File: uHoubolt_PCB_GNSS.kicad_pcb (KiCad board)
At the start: 4 copper layers, 85 x 80 mm, 89 parts, among them J1 Power In, J12 MMCX-J-P-H-RA-SM1, J2 Debug, J3 Debug, J4 CAN1, J5 CAN2, J6 CAN1, J7 CAN2, Q1 SISA88DN or similar, U1 SAM-M8Q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

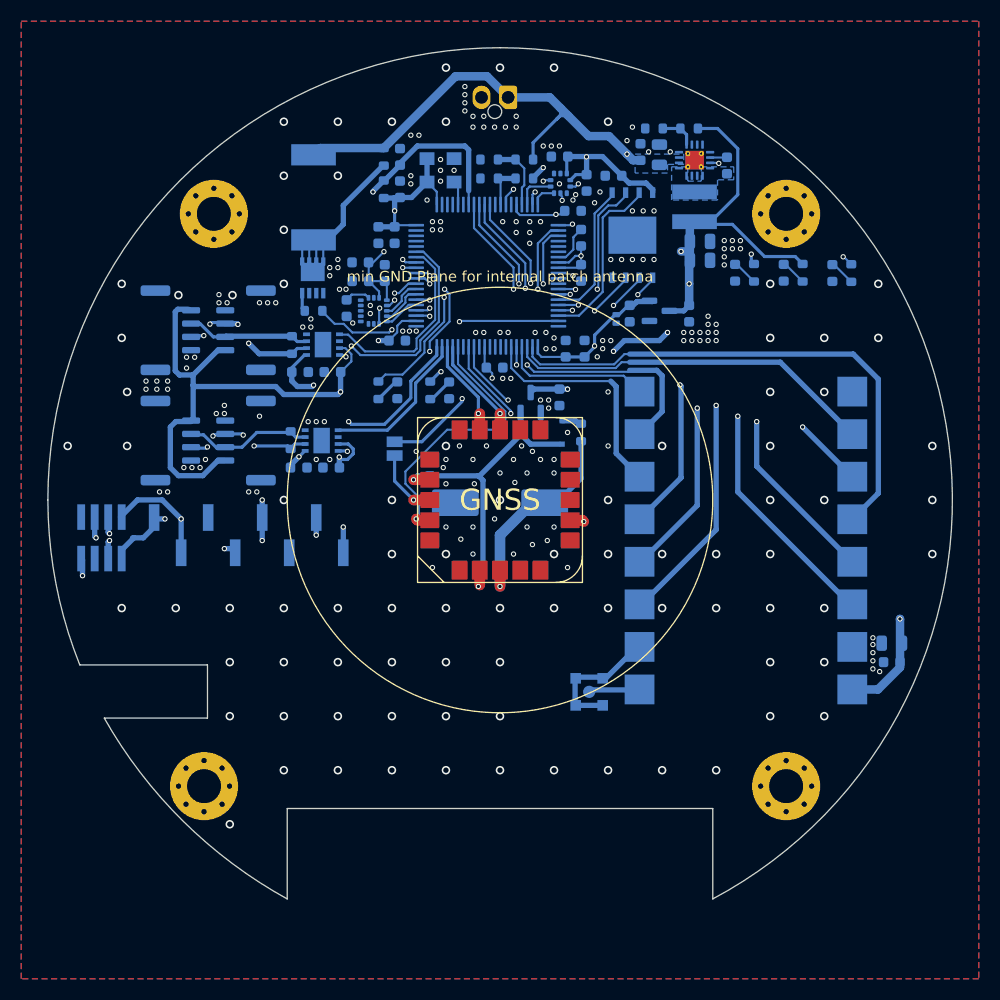
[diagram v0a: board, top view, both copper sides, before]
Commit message: Rounded board; updated LoRa module; Small bugfixes and rewiring
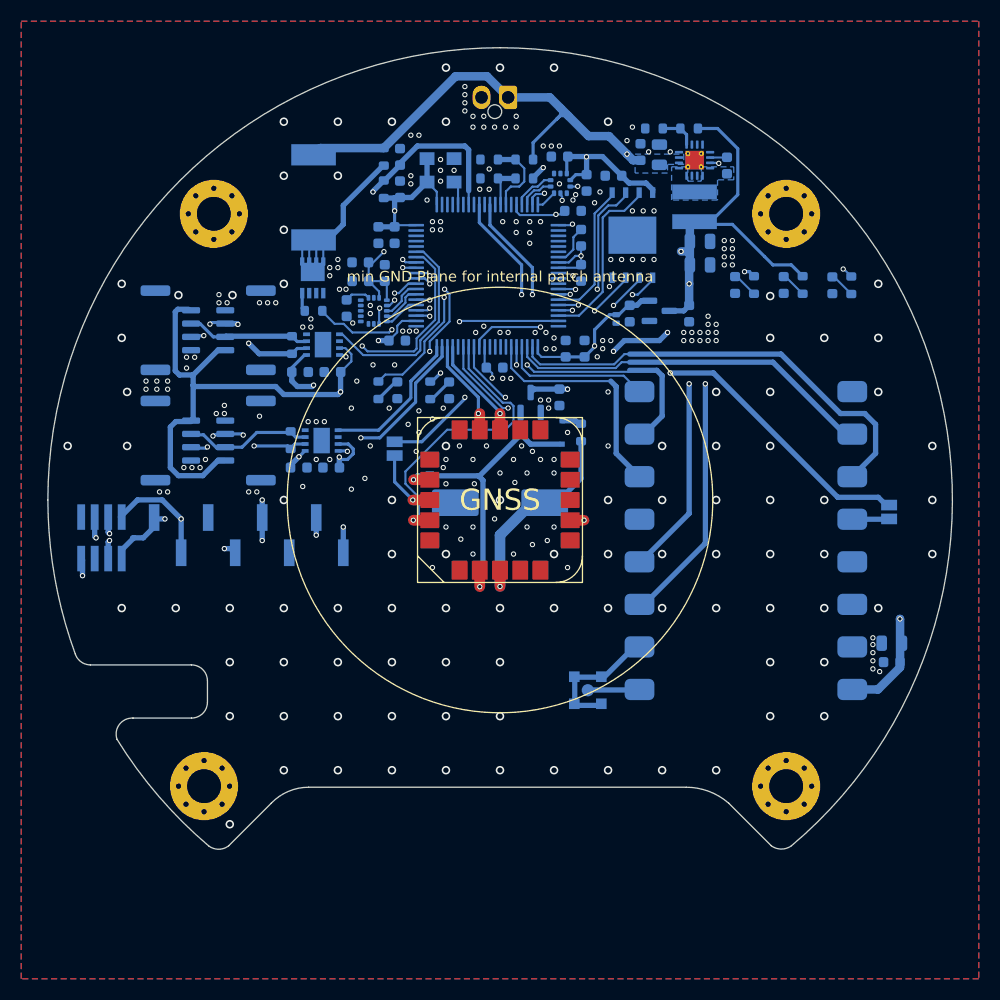
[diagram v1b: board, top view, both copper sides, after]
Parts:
- added JP2: SolderJumper_, Jumper:SolderJumper-2_P1.3mm_Open_Pad1.0x1.5mm, B.Cu at (186.6, 101.1)
- U10: value LoRa1278F30 -> LoRa1276F30; footprint TXV_Library_Footprints:G-NiceRF-LoRa1278F30 -> TXV_Library_Footprints:G-NiceRF-LoRa1268F30
- moved D3 1.15 mm to (176.7, 79.8)
- moved D5 1.15 mm to (172.1, 79.8)
- moved R14 1.15 mm to (178.4, 79.8)
- moved R17 1.15 mm to (173.9, 79.8)
- moved D1 1.15 mm to (181.2, 79.8)
- moved R6 1.15 mm to (183.0, 79.8)
- moved C24 0.43 mm to (168.8, 77.9)
- moved J12 0.20 mm to (158.3, 117.9)
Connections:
- net /5V_SNS renamed /5V_SENSE
- R7 pad 2: /12V_SNS -> /12V_SENSE
- R8 pad 1: /12V_SNS -> /12V_SENSE
- U1 pad 7: /GNSS_TPLS -> /GNSS_TIMEPULSE
- U10 pad 12: /LoRa_DIO2 -> unconnected-(U10-Pad12)
- U10 pad 14: /LoRa_DIO4 -> /LoRa_DIO3
- U10 pad 3: /LoRa_DIO5 -> unconnected-(U10-Pad3)
- U10 pad 4: /LoRa_DIO3 -> unconnected-(U10-Pad4)
- U10 pad 5: /LoRa_NRST -> Net-(U10-Pad5)
- U10 pad 6: /LoRa_DIO0 -> /LoRa_BUSY
- U2 pad 10: /LoRa_DIO2 -> unconnected-(U2-Pad10)
- U2 pad 14: /BARO_INT -> /12V_SENSE
- U2 pad 17: /12V_SNS -> /BARO_INT
- U2 pad 22: /LoRa_DIO4 -> unconnected-(U2-Pad22)
- U2 pad 23: /LoRa_DIO5 -> unconnected-(U2-Pad23)
- U2 pad 42: /LoRa_NRST -> /LoRa_BUSY
- U2 pad 52: unconnected-(U2-Pad52) -> /LoRa_NRST
- U2 pad 54: /GNSS_TPLS -> /GNSS_INT
- U2 pad 55: unconnected-(U2-Pad55) -> /GNSS_TIMEPULSE
- U2 pad 56: /GNSS_INT -> unconnected-(U2-Pad56)
- U2 pad 59: /CAN1_TX -> /CAN1_RX
- U2 pad 60: /CAN1_RX -> /CAN1_TX
- U2 pad 74: /CAN2_TX -> /CAN2_RX
- U2 pad 75: /CAN2_RX -> /CAN2_TX
- U2 pad 8: /LoRa_DIO0 -> unconnected-(U2-Pad8)
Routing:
- net /LoRa_DIO5: track 51.5 -> 0.00 mm, vias 2 -> 0
- net /LoRa_DIO4: track 49.8 -> 0.00 mm, vias 2 -> 0
- net /LoRa_DIO0: track 48.6 -> 0.00 mm, vias 2 -> 0
- net /LoRa_BUSY: track 0.00 -> 42.4 mm
- net /LoRa_DIO2: track 42.1 -> 0.00 mm, vias 2 -> 0
- net /GNSS_TIMEPULSE: track 0.00 -> 23.8 mm, vias 0 -> 2
- net /GNSS_TPLS: track 23.6 -> 0.00 mm, vias 2 -> 0
- net /12V_SENSE: track 0.00 -> 7.41 mm
- net /12V_SNS: track 6.32 -> 0.00 mm
- net Net-(U10-Pad5): track 0.00 -> 3.48 mm
- net /LoRa_NRST: track 49.3 -> 46.6 mm, vias 0 -> 2
- net /GNSS_INT: track 26.5 -> 28.2 mm
- net /CAN2_RX: track 20.2 -> 18.5 mm
- net /BARO_INT: track 5.57 -> 4.05 mm, vias 2 -> 0
- net /CAN2_TX: track 18.5 -> 19.9 mm
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- added copper zone on In2.Cu, net GND
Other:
- board size 85 x 80 mm -> 85 x 75.3 mm
- board text added: "RCU v1.0"
- board text removed: "IMRCU v0.1"
- board text removed: "Power State"
- board text removed: "System State"

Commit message: Changed MMCX Footprint, Moved mounting holes, moved prog connectors
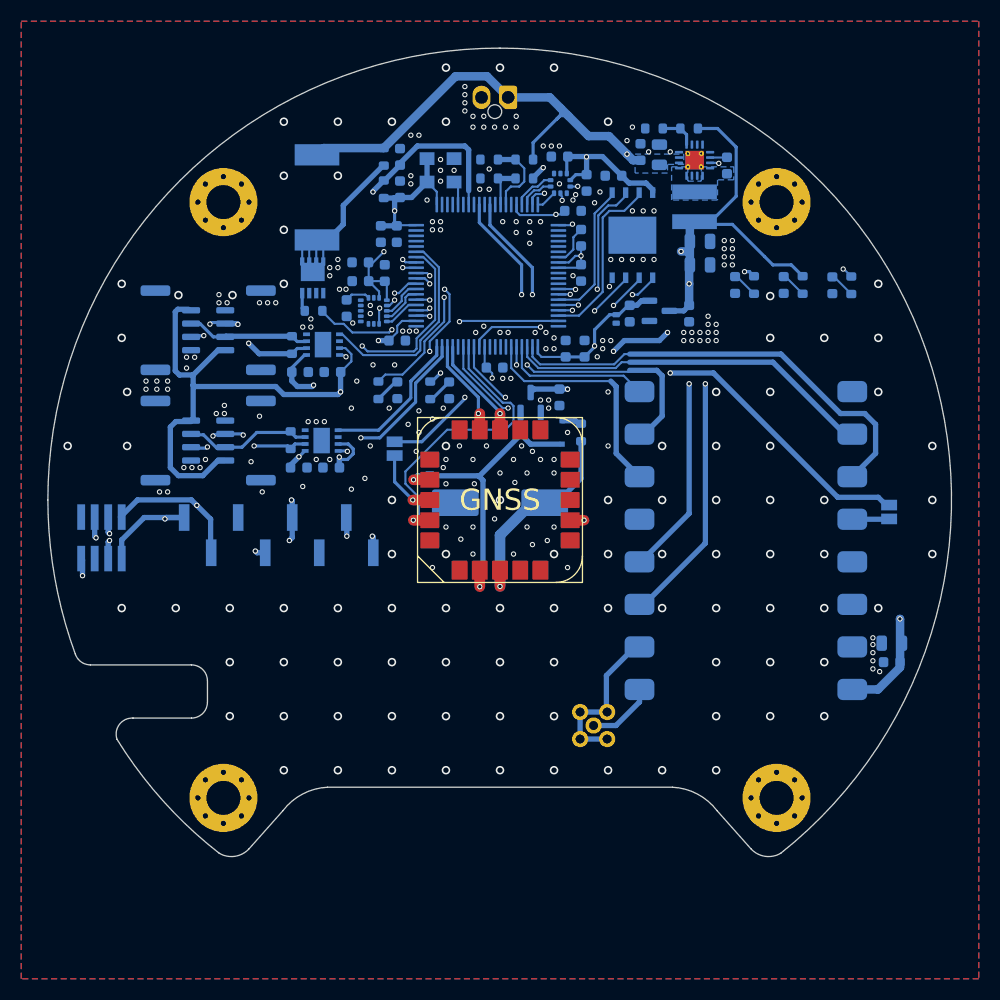
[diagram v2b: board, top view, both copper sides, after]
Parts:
- J12: footprint TXV_Library_Footprints:SAMTEC_MMCX-J-P-H-RA-SM1 -> TXV_Library_Footprints:MMCX_Horizontal_THT
- moved J12 3.36 mm to (158.8, 121.2), turned to 180 degrees
- moved J2 2.82 mm to (129.2, 103.3)
- moved H3 2.13 mm to (124.0, 128.0)
- moved H1 1.42 mm to (176.0, 72.0)
- moved H2 1.42 mm to (124.0, 72.0)
- moved H4 1.42 mm to (176.0, 128.0)
- moved LS1 0.33 mm to (132.8, 71.6)
- moved C10 0.25 mm to (138.8, 75.0)
- moved C5 0.23 mm to (140.3, 75.0)
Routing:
- net +3V3: track 239.1 -> 243.4 mm
- net /UART_RX: track 42.6 -> 46.5 mm
- net /NRST: track 75.2 -> 78.2 mm
- net Net-(J12-PadS1): track 12.4 -> 15.3 mm
- net /SWDIO: track 48.2 -> 50.4 mm
- net Net-(J12-Pad1): track 4.75 -> 6.41 mm
- net /SWCLK: track 56.9 -> 58.0 mm
- net /UART_TX: track 44.1 -> 45.0 mm
- net GND: vias 286 -> 288
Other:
- board size 85 x 75.3 mm -> 84.9 x 76 mm
- board text added: "+"
- board text removed: "LoRa asym HF"

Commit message: Cover
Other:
- board text added: "JLCJLCJLCJLC"
- board text added: "LED1"
- board text added: "LED2"
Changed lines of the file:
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@@
   (gr_line (start 147.714 87.677635) (end 137.046 87.677635) (layer "B.SilkS") (width 0.12))
   (gr_rect (start 109.806 99.746) (end 140.2 107.366) (layer "B.SilkS") (width 0.12) (fill none))
-  (gr_circle (center 150 100) (end 192.5 100) (layer "Dwgs.User") (width 0.12) (fill none))
+  (gr_circle (center 150 100) (end 193 100) (layer "Dwgs.User") (width 0.12) (fill none))
   (gr_circle (center 150 100) (end 170 100) (layer "Eco2.User") (width 0.12) (fill none))
   (gr_arc (start 121 115.5) (mid 122.06066 115.93934) (end 122.5 117) (layer "Edge.Cuts") (width 0.05))
-  (gr_arc (start 107.5 100) (mid 119.942011 69.948801) (end 150.000056 57.52334) (layer "Edge.Cuts") (width 0.05))
+  (gr_arc (start 107.5 100) (mid 119.942011 69.948802) (end 150.000056 57.52334) (layer "Edge.Cuts") (width 0.05))
   (gr_arc (start 111.5 115.5) (mid 110.622935 115.216863) (end 110.076975 114.474342) (layer "Edge.Cuts") (width 0.05))
   (gr_line (start 170.4 129.2) (end 173.6 132.8) (layer "Edge.Cuts") (width 0.05))
@@
   (gr_arc (start 176.4 133.2) (mid 174.929119 133.496164) (end 173.6 132.8) (layer "Edge.Cuts") (width 0.05))
   (gr_line (start 115.5 120.5) (end 121 120.5) (layer "Edge.Cuts") (width 0.05))
-  (gr_arc (start 150.000056 57.52334) (mid 190.074677 85.986398) (end 176.4 133.2) (layer "Edge.Cuts") (width 0.05))
+  (gr_arc (start 150.000056 57.52334) (mid 190.074677 85.986399) (end 176.4 133.2) (layer "Edge.Cuts") (width 0.05))
+  (gr_text "LED2" (at 141.9 89.7 90) (layer "B.SilkS")
+    (effects (font (size 1 1) (thickness 0.15)) (justify mirror))
+  )
   (gr_text "3V3" (at 172.352 82.347) (layer "B.SilkS")
     (effects (font (size 1 1) (thickness 0.15)) (justify mirror))
   )
-  (gr_text "CAN1" (at 113.678 85.268 90) (layer "B.SilkS")
+  (gr_text "CAN1" (at 113.678 84.2 90) (layer "B.SilkS")
     (effects (font (size 2 2) (thickness 0.5)) (justify mirror))
   )
@@
     (effects (font (size 2 2) (thickness 0.5)) (justify mirror))
   )
-  (gr_text "CAN2" (at 113.678 95.682 90) (layer "B.SilkS")
+  (gr_text "JLCJLCJLCJLC" (at 149 81.9) (layer "B.SilkS")
+    (effects (font (size 1 1) (thickness 0.15)) (justify mirror))
+  )
+  (gr_text "CAN2" (at 113.678 94.4 90) (layer "B.SilkS")
     (effects (font (size 2 2) (thickness 0.5)) (justify mirror))
   )
   (gr_text "1" (at 139.4 106) (layer "B.SilkS")
+    (effects (font (size 1 1) (thickness 0.15)) (justify mirror))
+  )
+  (gr_text "LED1" (at 146.8 89.7 90) (layer "B.SilkS")
     (effects (font (size 1 1) (thickness 0.15)) (justify mirror))
   )
@@
       (effects (font (size 1 1) (thickness 0.15)))
     )
+    (format (units 3) (units_format 1) (precision 4))
+    (style (thickness 0.1) (arrow_length 1.27) (text_position_mode 0) (extension_height 0.58642) (extension_offset 0.5) keep_text_aligned)
+  )
+  (dimension (type aligned) (layer "Eco2.User")
+    (pts (xy 192.4 100.1) (xy 107.5 100.1))
+    (height -49)
+    (gr_text "84,9000 mm" (at 149.95 147.95) (layer "Eco2.User")
+      (effects (font (size 1 1) (thickness 0.15)))
+    )

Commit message: RCU Release
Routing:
- net GND: vias 288 -> 287
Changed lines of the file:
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@@
       (layerselection 0x00010fc_ffffffff)
       (disableapertmacros false)
-      (usegerberextensions true)
+      (usegerberextensions false)
       (usegerberattributes true)
       (usegerberadvancedattributes true)
@@
   (via (at 171.844 75.616) (size 0.5) (drill 0.3) (layers "F.Cu" "B.Cu") (free) (net 1))
   (via (at 155.08 125.4) (size 0.8) (drill 0.5) (layers "F.Cu" "B.Cu") (free) (net 1))
-  (via (at 148.476 63.932) (size 0.5) (drill 0.3) (layers "F.Cu" "B.Cu") (free) (net 1))
   (via (at 118.758 89.586) (size 0.5) (drill 0.3) (layers "F.Cu" "B.Cu") (free) (net 1))
   (via (at 171.844 76.378) (size 0.5) (drill 0.3) (layers "F.Cu" "B.Cu") (free) (net 1))
